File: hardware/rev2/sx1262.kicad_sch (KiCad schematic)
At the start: 36 parts, among them U2 SX1262IMLTRT, U3 PE4259, Y2 TCXO 32MHz

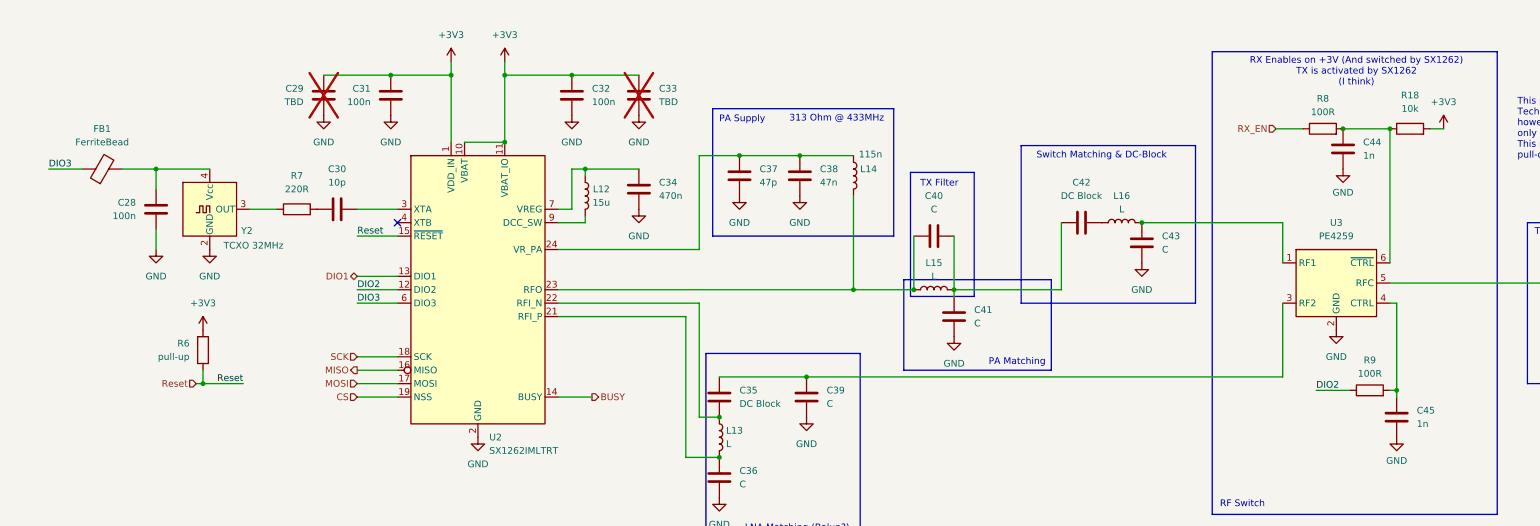
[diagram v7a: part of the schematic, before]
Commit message: redid usb termination and begun adding components from mouser
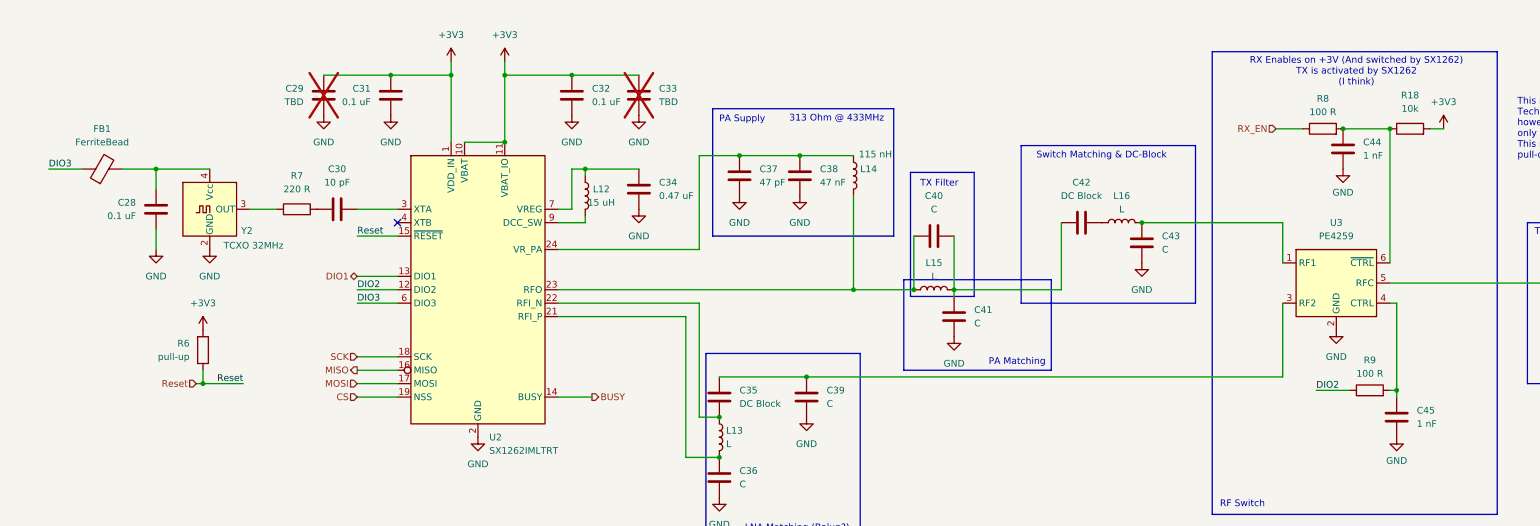
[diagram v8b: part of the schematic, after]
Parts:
- C28, C31, C32: value 100n -> 0.1 uF; Mouser Part Number (none) -> 81-GCJ188R71E104KA2D
- C30: value 10p -> 10 pF
- C34: value 470n -> 0.47 uF
- C37: value 47p -> 47 pF
- C38: value 47n -> 47 nF
- C44, C45: value 1n -> 1 nF
- L12: value 15u -> 15 uH
- L14: value 115n -> 115 nH
- R7: value 220R -> 220 R
- R8, R9: value 100R -> 100 R
- U2: Mouser Part Number (none) -> -
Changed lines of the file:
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@@
 			)
 		)
-		(property "Mouser Part Number" ""
+		(property "Mouser Part Number" "-"
 			(at 120.65 137.16 0)
 			(hide yes)
@@
 			)
 		)
-		(property "Value" "100n"
+		(property "Value" "0.1 uF"
 			(at 100.33 101.5999 0)
 			(show_name no)
@@
 			)
 		)
-		(property "Datasheet" ""
+		(property "Datasheet" "https://www.mouser.se/datasheet/3/76/1/GCJ188R71E104KA12_02B.pdf"
 			(at 104.14 100.33 0)
 			(hide yes)
@@
 			)
 		)
-		(property "Mouser Part Number" ""
+		(property "Mouser Part Number" " 81-GCJ188R71E104KA2D "
 			(at 104.14 100.33 0)
 			(hide yes)
@@
 			)
 		)
-		(property "Value" "100R"
+		(property "Value" "100 R"
 			(at 280.67 103.505 90)
 			(show_name no)
@@
 			)
 		)
-		(property "Value" "15u"
+		(property "Value" "15 uH"
 			(at 144.018 120.65 0)
 			(show_name no)
@@
 			)
 		)
-		(property "Value" "100n"
+		(property "Value" "0.1 uF"
 			(at 55.88 123.1899 0)
 			(show_name no)
@@
 			)
 		)
-		(property "Datasheet" ""
+		(property "Datasheet" "https://www.mouser.se/datasheet/3/76/1/GCJ188R71E104KA12_02B.pdf"
 			(at 59.69 121.92 0)
 			(hide yes)
@@
 			)
 		)
-		(property "Mouser Part Number" ""
+		(property "Mouser Part Number" " 81-GCJ188R71E104KA2D "
 			(at 59.69 121.92 0)
 			(hide yes)
@@
 			)
 		)
-		(property "Value" "100n"
+		(property "Value" "0.1 uF"
 			(at 142.24 101.5999 0)
 			(show_name no)
@@
 			)
 		)
-		(property "Datasheet" ""
+		(property "Datasheet" "https://www.mouser.se/datasheet/3/76/1/GCJ188R71E104KA12_02B.pdf"
 			(at 138.43 100.33 0)
 			(hide yes)
@@
 			)
 		)
-		(property "Mouser Part Number" ""
+		(property "Mouser Part Number" " 81-GCJ188R71E104KA2D "
 			(at 138.43 100.33 0)
 			(hide yes)
@@
 			)
 		)
-		(property "Value" "100R"
+		(property "Value" "100 R"
 			(at 289.56 153.035 90)
 			(show_name no)
@@
 			)
 		)
-		(property "Value" "220R"
+		(property "Value" "220 R"
 			(at 86.36 118.11 90)
 			(show_name no)
@@
 			)
 		)
-		(property "Value" "115n"
+		(property "Value" "115 nH"
 			(at 192.786 111.506 0)
 			(show_name no)
@@
 			)
 		)
-		(property "Value" "47p"
+		(property "Value" "47 pF"
 			(at 173.99 116.8399 0)
 			(show_name no)
@@
 			)
 		)
-		(property "Value" "47n"
+		(property "Value" "47 nF"
 			(at 185.42 116.8399 0)
 			(show_name no)
@@
 			)
 		)
-		(property "Value" "1n"
+		(property "Value" "1 nF"
 			(at 298.45 162.5599 0)
 			(show_name no)
@@
 			)
 		)
-		(property "Value" "1n"
+		(property "Value" "1 nF"
 			(at 288.29 111.7599 0)
 			(show_name no)
@@
 			)
 		)
-		(property "Value" "10p"
+		(property "Value" "10 pF"
 			(at 93.98 116.84 90)
 			(show_name no)
@@
 			)
 		)
-		(property "Value" "470n"
+		(property "Value" "0.47 uF"
 			(at 154.94 119.3799 0)
 			(show_name no)
